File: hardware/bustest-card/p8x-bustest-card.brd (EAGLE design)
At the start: 200 x 100 mm, 27 parts, among them J1 MABC96R, J2 PROBE 2x5, U1 MCP23S17, U2 MCP23S17, U3 MCP23S17, U4 MCP23S17, U5 MCP23S17, U6 74HCT244, U7 74HCT244

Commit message: refactor(bustest): back to a standard 160x100 Eurocard
The card was scoped at W=200 when it was ~45 parts, on the assumption it needed
the extra 40mm for the USB socket, probe header and LED bank. Three rounds of
cuts since -- the bus pull-down networks, the D0-7/A0-15 monitor LED arrays, and
the bus series resistors -- took it to 27 parts, and at 27 the extra width no
longer earns its place.

Auto-flow now fits everything in two rows on a standard Eurocard:

  edge  J1                                          x  1.7 -> 14.2
  row 1 U1-U7 + decoupling caps, A1 (Pico)          x 17.1 -> 150.0
  row 2 J2, D1, R5-R8, RPR/RST/RPRB, LPR/LST        x 17.1 -> 121.9

31% area utilisation, 10mm of slack at the outer edge, 0 parts overflowing the
outline, 0 footprint overlaps.

The mechanical argument is the real reason to go back. 200mm cantilevered off
the DIN connector is carried by just the two mounting holes at y=+/-45, and this
is the card that gets handled most -- every grabber clip and USB insertion puts
a moment through the connector. At 160mm it sits in the card guides like
everything else and the outer-standoff question disappears. Fab also gets one
panel size and one mechanical drawing across the whole set.

Nothing is lost: J1 still hugs the left edge with parts flowing +x, so the USB
socket, probe header and LED bank stay at the OUTER (reachable) end. That came
from the flow direction, not the extra width.

Every other board is byte-identical; the schematic is unchanged (outline size
does not affect it).

Co-Authored-By: Claude Opus 4.8 <noreply@anthropic.com>
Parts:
- moved D1 183.2 mm to (210.2, 42.6)
- moved J2 183.2 mm to (203.3, 42.7)
- moved R6 183.2 mm to (231.4, 42.7)
- moved R5 183.2 mm to (217.1, 42.7)
- moved CD2 40.0 mm to (231.4, 95.1)
- moved A1 40.0 mm to (316.8, 95.2)
- moved CD1 40.0 mm to (215.2, 95.1)
- moved CD3 40.0 mm to (247.6, 95.1)
- moved CD4 40.0 mm to (263.9, 95.1)
- moved CD5 40.0 mm to (280.1, 95.1)
- moved CD6 40.0 mm to (296.3, 95.1)
- moved CD7 40.0 mm to (312.5, 95.1)
- moved J1 40.0 mm to (193.3, 49.6)
- moved U1 40.0 mm to (203.3, 95.2)
- moved U2 40.0 mm to (219.5, 95.2)
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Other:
- board size 200 x 100 mm -> 160 x 100 mm

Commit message: feat(bustest): discrete limiting resistors instead of arrays
RPR/RST/RPRB were isolated resistor networks (RNISO8 / SIP-16). Replaced with
24 discrete axial resistors (R9-R32):

  R9-R16   330 ohm   buffered-LED series (U7 -> R -> LPR)
  R17-R24  330 ohm   status-LED series   (Pico -> R -> LST)
  R25-R32  1 kohm    probe series        (Pico -> R -> J2)

Why discrete and not a 9-pin SIP-8: these are series elements with a DIFFERENT
net on both ends of every leg, so a bussed SIP-8 (one shared COM pin) physically
cannot do the job -- it would short all eight legs together on the common side.
An isolated SIP-16 array works and is what was there, but discrete axials suit
an all-through-hole, hand-sourced bench card and were the chosen direction. The
pull-up networks elsewhere stay bussed SIP-9; those legs really do share VCC.

This is a deliberate part-count increase (27 -> 48). Recorded in BACKLOG WONT-DO
so it is not "simplified" back into a network without a reason that outweighs
the through-hole simplicity.

Verified: all 24 series paths connect the correct in/out nets, LED anodes and
probe-header pins land on the right resistor outputs, grounds intact, 0 nets
double-driven. Decoupling caps unchanged at 7 (that count follows IC count).
Auto-flow confirms 48 parts still fit 160x100 (5 rows, x_max 155/160). Docs and
the parts table updated; no other board touched.

Co-Authored-By: Claude Opus 4.8 <noreply@anthropic.com>
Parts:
- removed RPR, RST: 8x330R, p8x:SIP16
- removed RPRB: 8x1K, p8x:SIP16
- added R10, R11, R12, R13, R14, R15, R16, R17, R18, R19, R20, R21, R22, R23, R24, R9: 330R, p8x:R_AXIAL
- added R25, R26, R27, R28, R29, R30, R31, R32: 1K, p8x:R_AXIAL
- moved LST 12.6 mm to (286.3, 42.7)
- moved LPR 12.6 mm to (274.5, 42.7)
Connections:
- net LK_PR0: now also R9.2; no longer RPR.2
- net LK_PR1: now also R10.2; no longer RPR.4
- net LK_PR2: now also R11.2; no longer RPR.6
- net LK_PR3: now also R12.2; no longer RPR.8
- net LK_PR4: now also R13.2; no longer RPR.10
- net LK_PR5: now also R14.2; no longer RPR.12
- net LK_PR6: now also R15.2; no longer RPR.14
- net LK_PR7: now also R16.2; no longer RPR.16
- net L_PR0: now also R9.1; no longer RPR.1
- net L_PR1: now also R10.1; no longer RPR.3
- net L_PR2: now also R11.1; no longer RPR.5
- net L_PR3: now also R12.1; no longer RPR.7
- net L_PR4: now also R13.1; no longer RPR.9
- net L_PR5: now also R14.1; no longer RPR.11
- net L_PR6: now also R15.1; no longer RPR.13
- net L_PR7: now also R16.1; no longer RPR.15
- net PR0: now also R25.1; no longer RPRB.1
- net PR1: now also R26.1; no longer RPRB.3
- net PR2: now also R27.1; no longer RPRB.5
- net PR3: now also R28.1; no longer RPRB.7
- net PR4: now also R29.1; no longer RPRB.9
- net PR5: now also R30.1; no longer RPRB.11
- net PR6: now also R31.1; no longer RPRB.13
- net PR7: now also R32.1; no longer RPRB.15
- net PRJ0: now also R25.2; no longer RPRB.2
- net PRJ1: now also R26.2; no longer RPRB.4
- net PRJ2: now also R27.2; no longer RPRB.6
- net PRJ3: now also R28.2; no longer RPRB.8
- net PRJ4: now also R29.2; no longer RPRB.10
- net PRJ5: now also R30.2; no longer RPRB.12
- net PRJ6: now also R31.2; no longer RPRB.14
- net PRJ7: now also R32.2; no longer RPRB.16
- net ST0: now also R17.1; no longer RST.1
- net ST1: now also R18.1; no longer RST.3
- net ST2: now also R19.1; no longer RST.5
- net ST3: now also R20.1; no longer RST.7
- net ST4: now also R21.1; no longer RST.9
- net ST5: now also R22.1; no longer RST.11
- net ST6: now also R23.1; no longer RST.13
- net ST7: now also R24.1; no longer RST.15
- net STK0: now also R17.2; no longer RST.2
- net STK1: now also R18.2; no longer RST.4
- net STK2: now also R19.2; no longer RST.6
- net STK3: now also R20.2; no longer RST.8
- net STK4: now also R21.2; no longer RST.10
- net STK5: now also R22.2; no longer RST.12
- net STK6: now also R23.2; no longer RST.14
- net STK7: now also R24.2; no longer RST.16

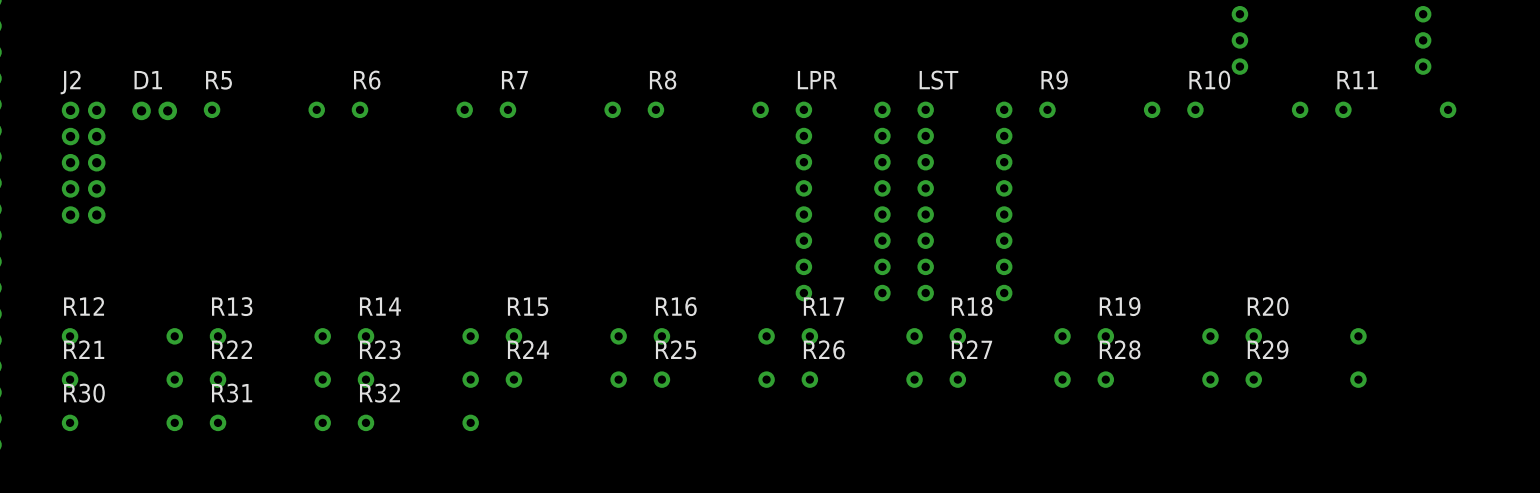
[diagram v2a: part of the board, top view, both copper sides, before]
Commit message: feat(bustest): individual labelled LEDs instead of bar arrays
LPR/LST (two LEDARR8 DIP-16 bar arrays) become 16 individual through-hole LEDs,
each silkscreen-labelled:

  LED1-8   probes    PROBE0-7      (via U7 74244 buffer, R9-R16)
  LED9-16  status    5V-OK, ARMED, LISTEN, CLK, CLKB, -RES, ERR, USB-ACT
                     (Pico GP7-GP14 direct, R17-R24)

Status meanings are bound in ST0..7 = GP7..GP14 order, which the netlist already
wires that way and the design doc §5.4 already lists in that order. The point of
individual parts is a printed name at every indicator -- worth it on a bench
tool read by glancing. Colors (probes green; status green/yellow/red by
severity) are provisional, tied to the §10 open item on the status set.

Deliberate part-count increase (48 -> 62), same standing as the discrete
resistors: recorded in BACKLOG WONT-DO so it is not re-arrayed without a reason
beating the labelled-through-hole clarity.

Verified: all 16 LED anode/cathode nets correct (probe anodes on LK_PRn, status
on STKn, all cathodes GND), no arrays left, labels present in the schematic.
Auto-flow confirms 62 parts still fit 160x100 (5 rows, x_max 156.8/160).
Decoupling caps unchanged at 7. Docs and parts table updated; no other board
touched.

Co-Authored-By: Claude Opus 4.8 <noreply@anthropic.com>
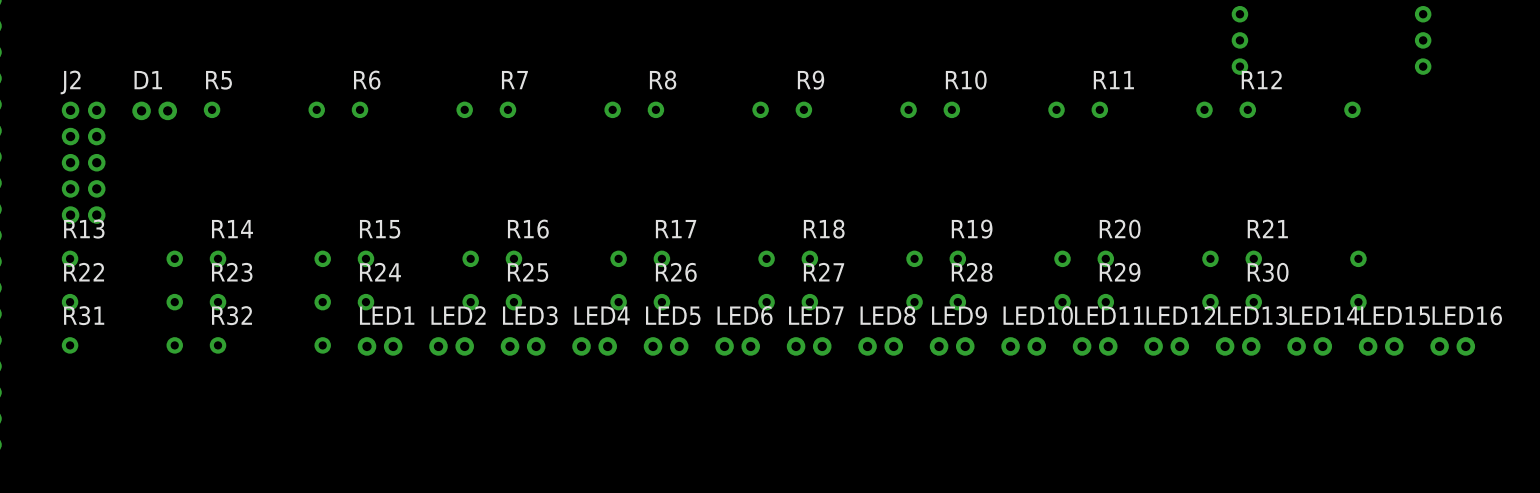
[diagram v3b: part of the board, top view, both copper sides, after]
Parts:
- removed LPR: PROBES, p8x:DIP16
- removed LST: STATUS, p8x:DIP16
- added LED1, LED10, LED11, LED16, LED2, LED3, LED4, LED5, LED6, LED7, LED8, LED9: GRN, p8x:LED5
- added LED12, LED13: YEL, p8x:LED5
- added LED14, LED15: RED, p8x:LED5
- moved R12 116.4 mm to (317.6, 42.7)
- moved R21 115.5 mm to (318.1, 28.3)
- moved R30 115.5 mm to (318.1, 24.1)
- moved R11 23.6 mm to (303.2, 42.7)
- moved R10 23.6 mm to (288.9, 42.7)
- moved R9 23.6 mm to (274.5, 42.7)
- moved R14 16.2 mm to (217.6, 28.3)
- moved R17 16.2 mm to (260.7, 28.3)
- moved R18 16.2 mm to (275.1, 28.3)
- moved R19 16.2 mm to (289.4, 28.3)
- moved R23 16.2 mm to (217.6, 24.1)
- moved R26 16.2 mm to (260.7, 24.1)
- moved R27 16.2 mm to (275.1, 24.1)
- moved R28 16.2 mm to (289.4, 24.1)
- moved R32 16.2 mm to (217.6, 19.9)
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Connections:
- net GND: now also LED1.1, LED10.1, LED11.1, LED12.1, LED13.1, LED14.1, LED15.1, LED16.1, LED2.1, LED3.1, LED4.1, LED5.1, LED6.1, LED7.1, LED8.1, LED9.1; no longer LPR.10, LPR.11, LPR.12, LPR.13, LPR.14, LPR.15, LPR.16, LPR.9, LST.10, LST.11, LST.12, LST.13, LST.14, LST.15, LST.16, LST.9
- net LK_PR0: now also LED1.2; no longer LPR.1
- net LK_PR1: now also LED2.2; no longer LPR.2
- net LK_PR2: now also LED3.2; no longer LPR.3
- net LK_PR3: now also LED4.2; no longer LPR.4
- net LK_PR4: now also LED5.2; no longer LPR.5
- net LK_PR5: now also LED6.2; no longer LPR.6
- net LK_PR6: now also LED7.2; no longer LPR.7
- net LK_PR7: now also LED8.2; no longer LPR.8
- net STK0: now also LED9.2; no longer LST.1
- net STK1: now also LED10.2; no longer LST.2
- net STK2: now also LED11.2; no longer LST.3
- net STK3: now also LED12.2; no longer LST.4
- net STK4: now also LED13.2; no longer LST.5
- net STK5: now also LED14.2; no longer LST.6
- net STK6: now also LED15.2; no longer LST.7
- net STK7: now also LED16.2; no longer LST.8

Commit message: feat(bustest): LED silk shows the function, not the color
The board silk was printing the LED color (GRN/RED/YEL). On a bench tool you
read by glancing, the useful thing next to each LED is what it MEANS. The
silkscreen VALUE is now the function:

  LED1-8   PROBE0 .. PROBE7
  LED9-16  5V-OK, ARMED, LISTEN, CLK, CLKB, -RES, ERR, USB-ACT

Color moves to the schematic label (provisional; §10 open item), so it is not
lost.

Required making the LED value-resolution color-aware. It used to split ANY
"FUNC-COLOR" value on the last hyphen (value=color, label=func), which would
mangle a hyphenated function name -- 5V-OK -> value "OK", -RES -> value "RES".
Now it splits only when the trailing token is a real color (LEDCOLORS set), so a
function passes through whole as the value. Verified this leaves every other
board's LED values byte-identical (control/led/alu/io/memory/regbank/cf all
unchanged): their values all end in GRN/RED/YEL, which still split as before.

No topology change; caps still 7; 62 parts still fit. Doc updated.

Co-Authored-By: Claude Opus 4.8 <noreply@anthropic.com>
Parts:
- LED1: value GRN -> PROBE0
- LED10: value GRN -> ARMED
- LED11: value GRN -> LISTEN
- LED12: value YEL -> CLK
- LED13: value YEL -> CLKB
- LED14: value RED -> -RES
- LED15: value RED -> ERR
- LED16: value GRN -> USB-ACT
- LED2: value GRN -> PROBE1
- LED3: value GRN -> PROBE2
- LED4: value GRN -> PROBE3
- LED5: value GRN -> PROBE4
- LED6: value GRN -> PROBE5
- LED7: value GRN -> PROBE6
- LED8: value GRN -> PROBE7
- LED9: value GRN -> 5V-OK
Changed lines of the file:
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@@
 <attribute name="VALUE" x="216.83" y="16.10" size="1.778" layer="27" ratio="10"/>
 </element>
-<element name="LED1" library="p8x" package="LED5" value="GRN" x="232.09" y="19.78" smashed="yes">
+<element name="LED1" library="p8x" package="LED5" value="PROBE0" x="232.09" y="19.78" smashed="yes">
 <attribute name="NAME" x="231.19" y="21.88" size="1.778" layer="25" ratio="10"/>
 <attribute name="VALUE" x="231.19" y="15.90" size="1.778" layer="27" ratio="10"/>
 </element>
-<element name="LED2" library="p8x" package="LED5" value="GRN" x="239.03" y="19.78" smashed="yes">
+<element name="LED2" library="p8x" package="LED5" value="PROBE1" x="239.03" y="19.78" smashed="yes">
 <attribute name="NAME" x="238.13" y="21.88" size="1.778" layer="25" ratio="10"/>
 <attribute name="VALUE" x="238.13" y="15.90" size="1.778" layer="27" ratio="10"/>
 </element>
-<element name="LED3" library="p8x" package="LED5" value="GRN" x="245.97" y="19.78" smashed="yes">
+<element name="LED3" library="p8x" package="LED5" value="PROBE2" x="245.97" y="19.78" smashed="yes">
 <attribute name="NAME" x="245.07" y="21.88" size="1.778" layer="25" ratio="10"/>
 <attribute name="VALUE" x="245.07" y="15.90" size="1.778" layer="27" ratio="10"/>
 </element>
-<element name="LED4" library="p8x" package="LED5" value="GRN" x="252.91" y="19.78" smashed="yes">
+<element name="LED4" library="p8x" package="LED5" value="PROBE3" x="252.91" y="19.78" smashed="yes">
 <attribute name="NAME" x="252.01" y="21.88" size="1.778" layer="25" ratio="10"/>
 <attribute name="VALUE" x="252.01" y="15.90" size="1.778" layer="27" ratio="10"/>
 </element>
-<element name="LED5" library="p8x" package="LED5" value="GRN" x="259.85" y="19.78" smashed="yes">
+<element name="LED5" library="p8x" package="LED5" value="PROBE4" x="259.85" y="19.78" smashed="yes">
 <attribute name="NAME" x="258.95" y="21.88" size="1.778" layer="25" ratio="10"/>
 <attribute name="VALUE" x="258.95" y="15.90" size="1.778" layer="27" ratio="10"/>
 </element>
-<element name="LED6" library="p8x" package="LED5" value="GRN" x="266.79" y="19.78" smashed="yes">
+<element name="LED6" library="p8x" package="LED5" value="PROBE5" x="266.79" y="19.78" smashed="yes">
 <attribute name="NAME" x="265.89" y="21.88" size="1.778" layer="25" ratio="10"/>
 <attribute name="VALUE" x="265.89" y="15.90" size="1.778" layer="27" ratio="10"/>
 </element>
-<element name="LED7" library="p8x" package="LED5" value="GRN" x="273.73" y="19.78" smashed="yes">
+<element name="LED7" library="p8x" package="LED5" value="PROBE6" x="273.73" y="19.78" smashed="yes">
 <attribute name="NAME" x="272.83" y="21.88" size="1.778" layer="25" ratio="10"/>
 <attribute name="VALUE" x="272.83" y="15.90" size="1.778" layer="27" ratio="10"/>
 </element>
-<element name="LED8" library="p8x" package="LED5" value="GRN" x="280.67" y="19.78" smashed="yes">
+<element name="LED8" library="p8x" package="LED5" value="PROBE7" x="280.67" y="19.78" smashed="yes">
 <attribute name="NAME" x="279.77" y="21.88" size="1.778" layer="25" ratio="10"/>
 <attribute name="VALUE" x="279.77" y="15.90" size="1.778" layer="27" ratio="10"/>
 </element>
-<element name="LED9" library="p8x" package="LED5" value="GRN" x="287.61" y="19.78" smashed="yes">
+<element name="LED9" library="p8x" package="LED5" value="5V-OK" x="287.61" y="19.78" smashed="yes">
 <attribute name="NAME" x="286.71" y="21.88" size="1.778" layer="25" ratio="10"/>
 <attribute name="VALUE" x="286.71" y="15.90" size="1.778" layer="27" ratio="10"/>
 </element>
-<element name="LED10" library="p8x" package="LED5" value="GRN" x="294.55" y="19.78" smashed="yes">
+<element name="LED10" library="p8x" package="LED5" value="ARMED" x="294.55" y="19.78" smashed="yes">
 <attribute name="NAME" x="293.65" y="21.88" size="1.778" layer="25" ratio="10"/>
 <attribute name="VALUE" x="293.65" y="15.90" size="1.778" layer="27" ratio="10"/>
 </element>
-<element name="LED11" library="p8x" package="LED5" value="GRN" x="301.49" y="19.78" smashed="yes">
+<element name="LED11" library="p8x" package="LED5" value="LISTEN" x="301.49" y="19.78" smashed="yes">
 <attribute name="NAME" x="300.59" y="21.88" size="1.778" layer="25" ratio="10"/>
 <attribute name="VALUE" x="300.59" y="15.90" size="1.778" layer="27" ratio="10"/>
 </element>
-<element name="LED12" library="p8x" package="LED5" value="YEL" x="308.43" y="19.78" smashed="yes">
+<element name="LED12" library="p8x" package="LED5" value="CLK" x="308.43" y="19.78" smashed="yes">
 <attribute name="NAME" x="307.53" y="21.88" size="1.778" layer="25" ratio="10"/>
 <attribute name="VALUE" x="307.53" y="15.90" size="1.778" layer="27" ratio="10"/>
 </element>
-<element name="LED13" library="p8x" package="LED5" value="YEL" x="315.37" y="19.78" smashed="yes">
+<element name="LED13" library="p8x" package="LED5" value="CLKB" x="315.37" y="19.78" smashed="yes">
 <attribute name="NAME" x="314.47" y="21.88" size="1.778" layer="25" ratio="10"/>
 <attribute name="VALUE" x="314.47" y="15.90" size="1.778" layer="27" ratio="10"/>
 </element>
-<element name="LED14" library="p8x" package="LED5" value="RED" x="322.31" y="19.78" smashed="yes">
+<element name="LED14" library="p8x" package="LED5" value="-RES" x="322.31" y="19.78" smashed="yes">
 <attribute name="NAME" x="321.41" y="21.88" size="1.778" layer="25" ratio="10"/>
 <attribute name="VALUE" x="321.41" y="15.90" size="1.778" layer="27" ratio="10"/>
 </element>
-<element name="LED15" library="p8x" package="LED5" value="RED" x="329.25" y="19.78" smashed="yes">
+<element name="LED15" library="p8x" package="LED5" value="ERR" x="329.25" y="19.78" smashed="yes">
 <attribute name="NAME" x="328.35" y="21.88" size="1.778" layer="25" ratio="10"/>
 <attribute name="VALUE" x="328.35" y="15.90" size="1.778" layer="27" ratio="10"/>
 </element>
-<element name="LED16" library="p8x" package="LED5" value="GRN" x="336.19" y="19.78" smashed="yes">
+<element name="LED16" library="p8x" package="LED5" value="USB-ACT" x="336.19" y="19.78" smashed="yes">
 <attribute name="NAME" x="335.29" y="21.88" size="1.778" layer="25" ratio="10"/>
 <attribute name="VALUE" x="335.29" y="15.90" size="1.778" layer="27" ratio="10"/>
